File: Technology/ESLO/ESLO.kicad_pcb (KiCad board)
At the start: 4 copper layers, 29 x 15 mm, 47 parts, among them J1 USB_B_Micro, J2 nRF24L01+, J3 Ibatt, J4 Board to Board, J5 Conn_01x10_Female, J6 Board to Board, SW1 RESET, U1 MAX1720, U10 ADS1294, U11 ATSAMD21G18A-AUT, U2 LP5907MFX-1.8, U3 LP5907MFX-3.0, U4 LP5907MFX-1.5, U5 TPS72301DDCT, U6 SN74AUP1G98, U7 MB85RS2MT, U8 MT29F2G01ABBGDWB-IT:G TR, U9 LSM303AGR, Y1 Crystal

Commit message: ESLO changelog
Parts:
- removed BT1: Coin Cell, Battery:BatteryHolder_Keystone_1058_1x2032
- removed C12: 10uF, Capacitor_SMD:C_0603_1608Metric
- removed the C13 at (168.6, 110.7)
- removed the C8 at (123.1, 59.7)
- removed D2: LED, LED_SMD:LED_0603_1608Metric
- removed the J2 at (185.3, 64.7)
- removed J3: Ibatt, TerminalBlock_4Ucon:TerminalBlock_4Ucon_1x02_P3.50mm_Horizontal
- removed J4, J6: Board to Board, Connector_Hirose:Hirose_DF52-6S-0.8H_1x06-1MP_P0.80mm_Horizontal
- removed JP1: Jumper, Connector_PinHeader_2.54mm:PinHeader_1x02_P2.54mm_Vertical
- removed the R2 at (108.9, 115.0)
- removed SW1: RESET, Button_Switch_SMD:SW_SPST_B3S-1000
- removed the U10 at (159.2, 83.6)
- removed the U4 at (126.8, 69.0)
- added ?: , , F.Cu at (161.5, 108.0)
- added C18: 1uF, Capacitor_SMD:C_0402_1005Metric, B.Cu at (157.4, 100.9)
- added C19: 0.1uF, Capacitor_SMD:C_0402_1005Metric, B.Cu at (157.4, 102.3)
- added C20: 1uF, Capacitor_SMD:C_0402_1005Metric, B.Cu at (166.0, 113.3)
- added C21: 0.1uF, Capacitor_SMD:C_0402_1005Metric, B.Cu at (166.0, 112.2)
- added C22: 4.7nF, Capacitor_SMD:C_0402_1005Metric, B.Cu at (167.9, 104.4)
- added C23: 4.7nF, Capacitor_SMD:C_0402_1005Metric, B.Cu at (167.9, 106.8)
- added C24: 1000pF, Capacitor_SMD:C_0402_1005Metric, B.Cu at (167.1, 102.3)
- added C25: 4.7nF, Capacitor_SMD:C_0402_1005Metric, B.Cu at (167.8, 109.4)
- added C26: 4.7nF, Capacitor_SMD:C_0402_1005Metric, B.Cu at (167.8, 111.9)
- added C27: 1uF, Capacitor_SMD:C_0402_1005Metric, B.Cu at (159.7, 102.3)
- added C28: 0.1uF, Capacitor_SMD:C_0402_1005Metric, B.Cu at (159.7, 100.9)
- added C29: 10nF, Capacitor_SMD:C_0402_1005Metric, F.Cu at (155.9, 106.8)
- added C3: 1uF, Capacitor_SMD:C_0402_1005Metric, B.Cu at (156.3, 112.0)
- added C30: 1nF, Capacitor_SMD:C_0402_1005Metric, F.Cu at (155.9, 108.0)
- added C31: 22uF, Capacitor_SMD:C_0603_1608Metric, B.Cu at (161.2, 112.7)
- added C32: 1uF, Capacitor_SMD:C_0402_1005Metric, B.Cu at (158.5, 112.6)
- added C33: 0.1uF, Capacitor_SMD:C_0402_1005Metric, B.Cu at (162.2, 100.9)
- added C34: 1uF, Capacitor_SMD:C_0402_1005Metric, B.Cu at (162.2, 102.3)
- added C35: 1uF, Capacitor_SMD:C_0402_1005Metric, B.Cu at (163.9, 112.7)
- added C36: 1nF, Capacitor_SMD:C_0402_1005Metric, B.Cu at (169.4, 102.3)
- added C37: 4.7pF, Capacitor_SMD:C_0402_1005Metric, F.Cu at (148.6, 109.1)
- added C38: 2.2nF, Capacitor_SMD:C_0402_1005Metric, F.Cu at (150.5, 109.1)
- added C39: 1.5pF, Capacitor_SMD:C_0402_1005Metric, F.Cu at (147.5, 111.2)
- added C4: 22pF, Capacitor_SMD:C_0402_1005Metric, F.Cu at (165.1, 101.4)
- added C40: 1pF, Capacitor_SMD:C_0402_1005Metric, F.Cu at (147.5, 110.1)
- added C41: 33nF, Capacitor_SMD:C_0402_1005Metric, F.Cu at (150.6, 113.3)
- added C42: 22pF, Capacitor_SMD:C_0402_1005Metric, F.Cu at (151.1, 106.8)
- added C43: 22pF, Capacitor_SMD:C_0402_1005Metric, F.Cu at (151.1, 108.0)
- added L1: 2.7nH, Inductor_SMD:L_0402_1005Metric, F.Cu at (149.5, 110.1)
- added L2: 8.2nH, Inductor_SMD:L_0402_1005Metric, F.Cu at (151.0, 110.7)
- added L3: 3.9nH, Inductor_SMD:L_0402_1005Metric, F.Cu at (149.5, 111.2)
- added NT1: Net-Tie_2, NetTie:NetTie-2_SMD_Pad0.5mm, F.Cu at (153.6, 103.7)
- added R10: 4.7k, LED_SMD:LED_0402_1005Metric, B.Cu at (169.4, 104.9)
- added R11: 4.7k, LED_SMD:LED_0402_1005Metric, B.Cu at (169.4, 103.8)
- added R12: 4.7k, LED_SMD:LED_0402_1005Metric, B.Cu at (169.4, 107.4)
- added R13: 1M, LED_SMD:LED_0402_1005Metric, B.Cu at (167.1, 100.9)
- added R14: 4.7k, LED_SMD:LED_0402_1005Metric, B.Cu at (169.4, 106.2)
- added R15: 4.7k, LED_SMD:LED_0402_1005Metric, B.Cu at (169.4, 109.9)
- added R16: 4.7k, Resistor_SMD:R_0402_1005Metric, B.Cu at (169.4, 108.8)
- added R17: 4.7k, Resistor_SMD:R_0402_1005Metric, B.Cu at (169.4, 112.5)
- added R18: 4.7k, Resistor_SMD:R_0402_1005Metric, B.Cu at (169.4, 111.3)
- added R19: 22k, LED_SMD:LED_0402_1005Metric, F.Cu at (150.6, 112.2)
- added R3: 4.7k, Resistor_SMD:R_0402_1005Metric, F.Cu at (165.3, 111.7)
- added R4: 100k, LED_SMD:LED_0402_1005Metric, F.Cu at (153.1, 105.3)
- added R9: 100k, LED_SMD:LED_0402_1005Metric, F.Cu at (154.7, 105.0)
- added U1: LP5907MFX-1.8, Package_TO_SOT_SMD:SOT-23-5, F.Cu at (156.2, 101.9)
- added U11: nRF24L01P, Package_DFN_QFN:QFN-20-1EP_4x4mm_P0.5mm_EP2.5x2.5mm, F.Cu at (154.2, 111.2)
- added U12: AN91445, ARBO Parts:AN91445_MG, F.Cu at (144.6, 106.9)
- added Y2: SXT21412AA16, MyAntennas:SXT214, F.Cu at (154.2, 106.8)
- C10, C2, U5: moved to B.Cu
- C11: renamed from C9; moved to B.Cu
- C14: value 100nF -> 10uF; footprint Capacitor_SMD:C_0402_1005Metric -> Capacitor_SMD:C_0603_1608Metric
- C15: value 22pF -> 220nF
- C16: value 22pF -> 1uF; moved to B.Cu
- C17: value 1uF -> 0.1uF; moved to B.Cu
- C5: value 1uF -> 22pF
- C7: renamed from C1; moved to B.Cu
- C8: renamed from C4; moved to B.Cu
- C9: renamed from C7; moved to B.Cu
- J1: value USB_B_Micro -> Board to Board; footprint Connector_USB:USB_Micro-B_Molex-105017-0001 -> Connector_Hirose:Hirose_DF52-6S-0.8H_1x06-1MP_P0.80mm_Horizontal
- R5: value 4.7k -> 100k; footprint Resistor_SMD:R_0402_1005Metric -> LED_SMD:LED_0402_1005Metric
- R6: renamed from R3; moved to B.Cu
- R8: renamed from R4; moved to B.Cu
- U2: value LP5907MFX-1.8 -> LP5907MFX-1.5; moved to B.Cu
- U3: value LP5907MFX-3.0 -> MT29F2G01ABBGDWB-IT:G TR; footprint Package_TO_SOT_SMD:SOT-23-5 -> ARBO Parts:8x6mm_WSON_UTSO; moved to B.Cu
- U4: renamed from U1; moved to B.Cu
- U7: value MB85RS2MT -> LSM303AGR; footprint Package_DFN_QFN:DFN-8-1EP_3x3mm_P0.65mm_EP1.7x2.05mm -> Package_LGA:LGA-12_2x2mm_P0.5mm
- U8: value MT29F2G01ABBGDWB-IT:G TR -> CY15V104QI-20LPXC; footprint ARBO Parts:8x6mm_WSON_UTSO -> Package_DFN_QFN:DFN-8-1EP_3x3mm_P0.65mm_EP1.7x2.05mm; moved to B.Cu
- U9: value LSM303AGR -> ADS1294; footprint Package_LGA:LGA-12_2x2mm_P0.5mm -> ARBO Parts:BGA-64_8x8_8.0x8.0mm_ADS129x; moved to B.Cu
- moved D1 60.4 mm to (169.3, 112.9)
- moved C10 57.5 mm to (154.6, 109.1), turned to 180 degrees
- moved R8 56.8 mm to (156.8, 107.8), turned to 180 degrees
- moved R5 56.8 mm to (151.1, 105.3)
- moved C11 56.6 mm to (152.5, 109.1), turned to 180 degrees
- moved C1 55.9 mm to (158.8, 101.3), turned to 270 degrees
- moved C7 53.7 mm to (156.4, 103.5), turned to 180 degrees
- moved C8 52.5 mm to (156.4, 104.7)
- moved U9 52.4 mm to (162.3, 107.3), turned to 180 degrees
- moved R2 51.8 mm to (165.3, 113.0), turned to 180 degrees
- moved C14 50.9 mm to (158.5, 112.9)
- moved C5 48.1 mm to (159.8, 101.3), turned to 90 degrees
- moved C15 47.7 mm to (158.0, 111.5), turned to 180 degrees
- moved U4 45.6 mm to (153.4, 102.4), turned to 90 degrees
- moved U5 45.3 mm to (153.4, 106.4), turned to 90 degrees
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- renumbered C3 to C1, C11 to C13, J5 to J2, R6 to R2, U6 to U10, U11 to U6
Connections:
- C1 pad 2: GNDA -> GNDD
- C13 pad 2: GNDA -> GNDD
- C14 pad 2: GNDA -> GNDD
- C15 pad 1: Net-(C15-Pad1) -> GNDD
- C15 pad 2: GNDA -> Net-(C15-Pad2)
- C16 pad 1: GNDA -> VDDA
- C16 pad 2: Net-(C16-Pad2) -> GNDA
- C17 pad 1: GNDA -> VDDA
- C17 pad 2: Net-(C17-Pad2) -> GNDA
- C2 pad 1: Net-(BT1-Pad2) -> GNDA
- C2 pad 2: Net-(C2-Pad2) -> +1V8
- C5 pad 1: Net-(C5-Pad1) -> GNDD
- C5 pad 2: Net-(BT1-Pad2) -> Net-(C5-Pad2)
- C6 pad 1: GNDA -> GNDD
- C6 pad 2: +1V8 -> Net-(C6-Pad2)
- D1 pad 2: Net-(C5-Pad1) -> LED13
- J1 pad 1: Net-(C2-Pad2) -> +BATT
- J1 pad 2: D- -> Net-(J1-Pad2)
- J1 pad 3: D+ -> Net-(J1-Pad3)
- J1 pad 4: (no net) -> TEMP
- J1 pad 5: Net-(BT1-Pad2) -> Net-(J1-Pad5)
- J1 pad 6: Net-(BT1-Pad2) -> GNDD
- J2 pad 1: (no net) -> Net-(J2-Pad1)
- J2 pad 10: (no net) -> Net-(C24-Pad1)
- J2 pad 2: (no net) -> Net-(J2-Pad2)
- J2 pad 3: (no net) -> Net-(J2-Pad3)
- J2 pad 4: (no net) -> Net-(J2-Pad4)
- J2 pad 5: (no net) -> Net-(J2-Pad5)
- J2 pad 6: (no net) -> Net-(J2-Pad6)
- J2 pad 7: (no net) -> Net-(J2-Pad7)
- J2 pad 8: (no net) -> Net-(J2-Pad8)
- R1 pad 1: Net-(C2-Pad2) -> Net-(D1-Pad1)
- R1 pad 2: Net-(R1-Pad2) -> GNDD
- R5 pad 1: Net-(D2-Pad1) -> R_VBATT
- R5 pad 2: GNDA -> GNDD
- R7 pad 1: +1V8 -> ~SHDN
- R7 pad 2: SCL -> GNDD
- U10 pad 2: GNDA -> GNDD
- U10 pad 3: (no net) -> EEG_CS
- U10 pad 4: (no net) -> Net-(U10-Pad4)
- U2 pad 1: +BATT -> +1V8
- U2 pad 3: +BATT -> ~SHDN
- U2 pad 5: +1V8 -> VDDA
- U3 pad 1: Net-(C2-Pad2) -> (no net)
- U3 pad 2: Net-(BT1-Pad2) -> MISO
- U3 pad 3: Net-(R1-Pad2) -> (no net)
- U3 pad 4: (no net) -> GNDD
- U3 pad 5: Net-(C5-Pad1) -> MOSI
- U6 pad 1: Net-(C16-Pad2) -> Net-(C5-Pad2)
- U6 pad 12: (no net) -> R_VBATT
- U6 pad 18: GNDA -> GNDD
- U6 pad 2: Net-(C15-Pad1) -> Net-(C4-Pad1)
- U6 pad 21: (no net) -> MISO
- U6 pad 3: (no net) -> TEMP
- U6 pad 30: Net-(J6-Pad5) -> Net-(J1-Pad5)
- U6 pad 33: Net-(J6-Pad2) -> Net-(J1-Pad2)
- U6 pad 34: Net-(J6-Pad3) -> Net-(J1-Pad3)
- U6 pad 35: GNDA -> GNDD
- U6 pad 42: GNDA -> GNDD
- U6 pad 43: Net-(C17-Pad2) -> Net-(C6-Pad2)
- U6 pad 5: GNDA -> GNDD
- U7 pad 1: (no net) -> SCL
- U7 pad 2: MISO -> +1V8
- U7 pad 3: (no net) -> +1V8
- U7 pad 4: GNDA -> SDA
- U7 pad 5: MOSI -> Net-(C15-Pad2)
- U7 pad 6: SCK -> GNDD
- U7 pad 8: +1V8 -> GNDD
- U7 pad 9: (no net) -> +1V8
- U8 pad 4: GNDA -> GNDD
- Y1 pad 1: Net-(C15-Pad1) -> Net-(C4-Pad1)
- Y1 pad 2: Net-(C16-Pad2) -> Net-(C5-Pad2)
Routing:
- net GNDA: track 0.00 -> 40.9 mm, vias 0 -> 1
- net +1V8: track 0.00 -> 39.5 mm, vias 0 -> 3
- net ~SHDN: track 0.00 -> 33.7 mm, vias 0 -> 5
- net MISO: track 0.00 -> 29.7 mm, vias 0 -> 2
- net VDDA: track 0.00 -> 23.3 mm, vias 0 -> 2
- net MOSI: track 0.00 -> 20.1 mm, vias 0 -> 3
- net VSSA: track 0.00 -> 14.7 mm, vias 0 -> 12
- net SCK: track 0.00 -> 13.4 mm, vias 0 -> 2
- net GNDD: track 0.00 -> 11.1 mm, vias 0 -> 26
- net Net-(C11-Pad2): track 0.00 -> 10.8 mm, vias 0 -> 2
- net Net-(C8-Pad1): track 0.00 -> 10.6 mm
- net Net-(C36-Pad1): track 0.00 -> 7.44 mm, vias 0 -> 2
- net Net-(C24-Pad1): track 0.00 -> 6.72 mm, vias 0 -> 1
- net Net-(C22-Pad2): track 0.00 -> 6.58 mm, vias 0 -> 2
- net Net-(C24-Pad2): track 0.00 -> 5.92 mm, vias 0 -> 2
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- added copper zone on F.Cu, net GNDD
- added copper zone on GNDD, net GNDD
- added copper zone on VSSA, net GNDD
- added copper zone on VSSA, net VSSA
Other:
- board size 29 x 15 mm -> 32 x 14 mm
- net class Default: clearance 0.2 -> 0.15; trace_width 0.127 -> 0.15
- rule trace_clearance: 0.2 -> 0.15
- rule trace_min: 0.127 -> 0.15
- rule via_min_drill: 0.2 -> 0.1
- rule via_min_size: 0.4 -> 0.254

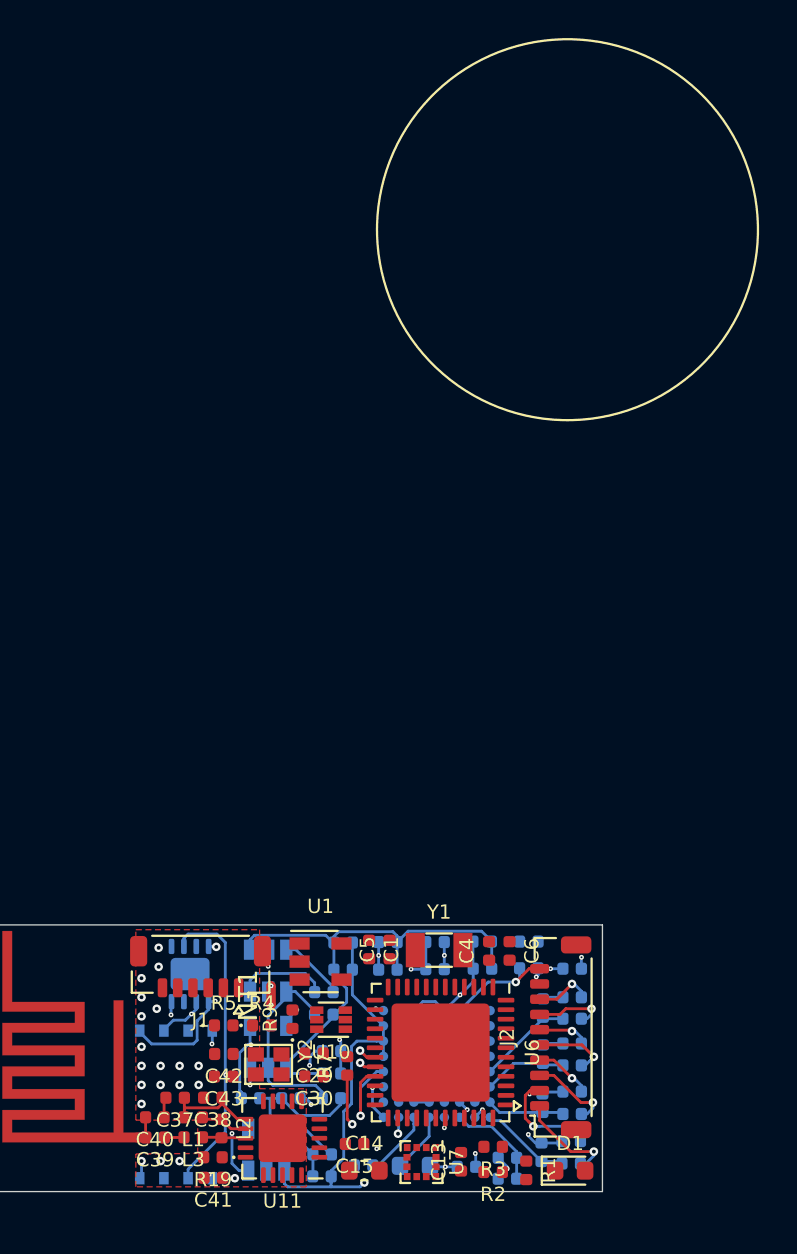
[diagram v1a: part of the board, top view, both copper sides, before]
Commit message: Added ESLO debugger and PSP
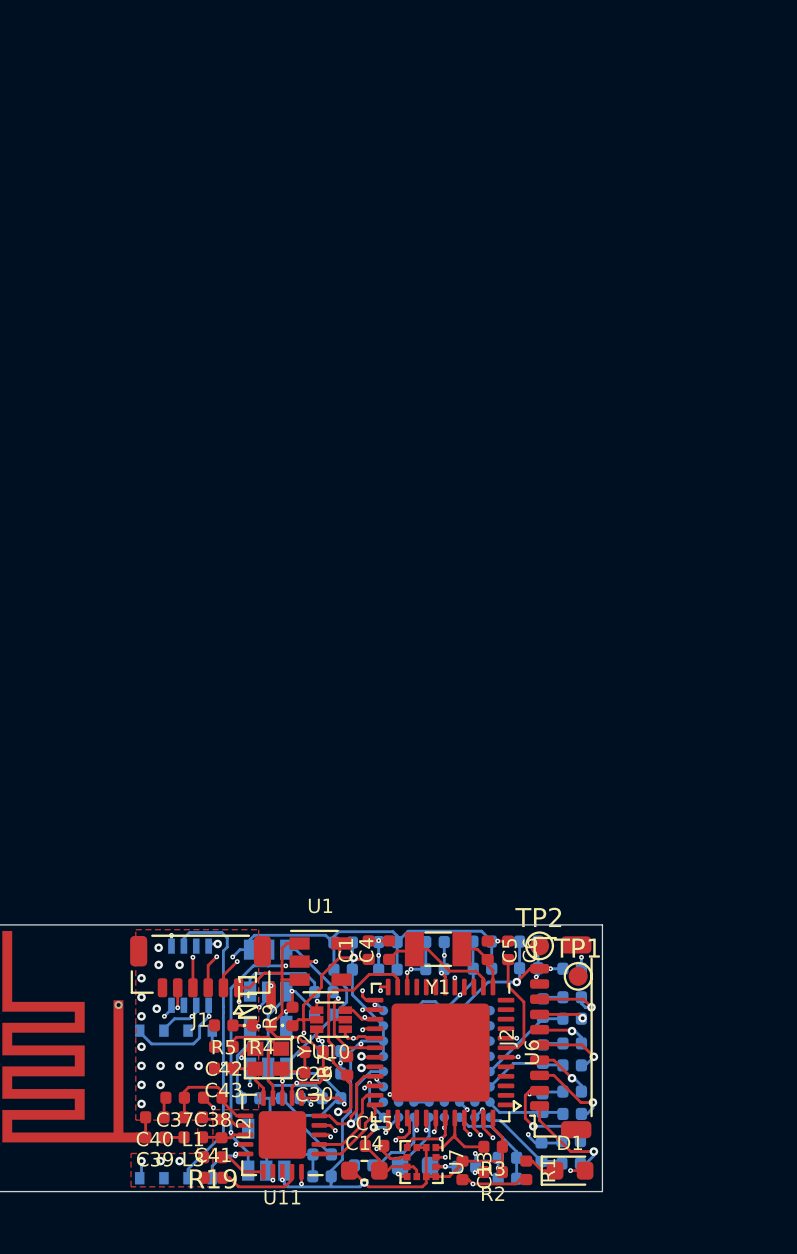
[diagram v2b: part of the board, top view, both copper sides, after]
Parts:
- removed ?: , 
- added TP1: TestPoint, TestPoint:TestPoint_Pad_D1.0mm, F.Cu at (169.7, 102.7)
- added TP2: TestPoint, TestPoint:TestPoint_Pad_D1.0mm, F.Cu at (167.7, 101.1)
- C13: value 100nF -> 0.1uF
- R10, R11, R12, R13, R14, R15, R19: footprint LED_SMD:LED_0402_1005Metric -> Resistor_SMD:R_0402_1005Metric
- U8: footprint Package_DFN_QFN:DFN-8-1EP_3x3mm_P0.65mm_EP1.7x2.05mm -> ARBO Parts:8-GQFN_FRAM_3.28mm-3.23mm
- moved C4 5.25 mm to (159.8, 101.3)
- moved C5 5.15 mm to (165.0, 101.3), turned to 270 degrees
- moved C15 1.05 mm to (159.0, 111.6), turned to 0 degrees
- moved C13 0.46 mm to (163.7, 112.9), turned to 270 degrees
- moved C43 0.43 mm to (151.1, 107.5)
- moved C42 0.38 mm to (151.1, 106.4)
- moved Y2 0.30 mm to (154.1, 106.5)
- moved C30 0.20 mm to (155.9, 107.8)
- moved U11 0.17 mm to (154.2, 111.0)
- moved R9 0.14 mm to (154.7, 104.8)
- moved C6 0.08 mm to (166.1, 101.3)
- moved C29 0.08 mm to (155.9, 106.7)
- moved Y1 0.07 mm to (162.4, 101.3), turned to 180 degrees
- turned C1 to 90 degrees
- turned C41 to 0 degrees
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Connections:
- net Net-(J1-Pad2) renamed D-
- net Net-(J1-Pad3) renamed D+
- C29 pad 1: Net-(C29-Pad1) -> +BATT
- C30 pad 1: Net-(C29-Pad1) -> +BATT
- J1 pad 5: Net-(J1-Pad5) -> DEBUG
- U11 pad 1: (no net) -> RF_CE
- U11 pad 15: Net-(C29-Pad1) -> +BATT
- U11 pad 18: Net-(C29-Pad1) -> +BATT
- U11 pad 2: (no net) -> RF_CSN
- U11 pad 6: (no net) -> RF_IRQ
- U11 pad 7: Net-(C29-Pad1) -> +BATT
- U3 pad 1: (no net) -> NAND_CS
- U6 pad 10: (no net) -> TEMP
- U6 pad 11: (no net) -> ~SHDN
- U6 pad 13: (no net) -> FRAM_CS
- U6 pad 14: (no net) -> NAND_CS
- U6 pad 15: (no net) -> EEG_CS
- U6 pad 16: (no net) -> EEG_DRDY
- U6 pad 22: (no net) -> EEG_START
- U6 pad 23: (no net) -> RF_CSN
- U6 pad 24: (no net) -> RF_CE
- U6 pad 25: (no net) -> RF_IRQ
- U6 pad 27: (no net) -> DEBUG
- U6 pad 28: (no net) -> MAG_INT
- U6 pad 29: (no net) -> INT2_XL
- U6 pad 3: TEMP -> (no net)
- U6 pad 30: Net-(J1-Pad5) -> INT1_XL
- U6 pad 45: (no net) -> SWCLK
- U6 pad 46: (no net) -> SWDIO
- U7 pad 11: (no net) -> INT2_XL
- U7 pad 12: (no net) -> INT1_XL
- U7 pad 7: (no net) -> MAG_INT
- U8 pad 1: (no net) -> FRAM_CS
- U9 pad 6D: (no net) -> EEG_DRDY
- U9 pad 7G: (no net) -> EEG_START
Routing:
- net +1V8: track 39.5 -> 81.8 mm, vias 3 -> 10
- net +BATT: track 0.00 -> 28.8 mm, vias 0 -> 6
- net D+: track 0.00 -> 28.7 mm, vias 0 -> 2
- net GNDD: track 11.1 -> 39.6 mm, vias 26 -> 39
- net D-: track 0.00 -> 26.3 mm, vias 0 -> 2
- net DEBUG: track 0.00 -> 23.7 mm, vias 0 -> 2
- net TEMP: track 0.00 -> 15.6 mm, vias 0 -> 3
- net NAND_CS: track 0.00 -> 15.3 mm, vias 0 -> 3
- net ~SHDN: track 33.7 -> 48.2 mm
- net FRAM_CS: track 0.00 -> 13.0 mm, vias 0 -> 3
- net LED13: track 0.00 -> 11.6 mm, vias 0 -> 2
- net R_VBATT: track 0.00 -> 10.3 mm, vias 0 -> 2
- net SCK: track 13.4 -> 22.9 mm, vias 2 -> 4
- net EEG_CS: track 0.00 -> 6.80 mm, vias 0 -> 3
- net Net-(U10-Pad4): track 0.00 -> 6.76 mm, vias 0 -> 3
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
